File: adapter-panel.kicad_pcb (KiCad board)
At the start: 2 copper layers, 61 x 98.9 mm, 8 parts, among them J1 GPIB_Connector, U1 ArduioProMicro

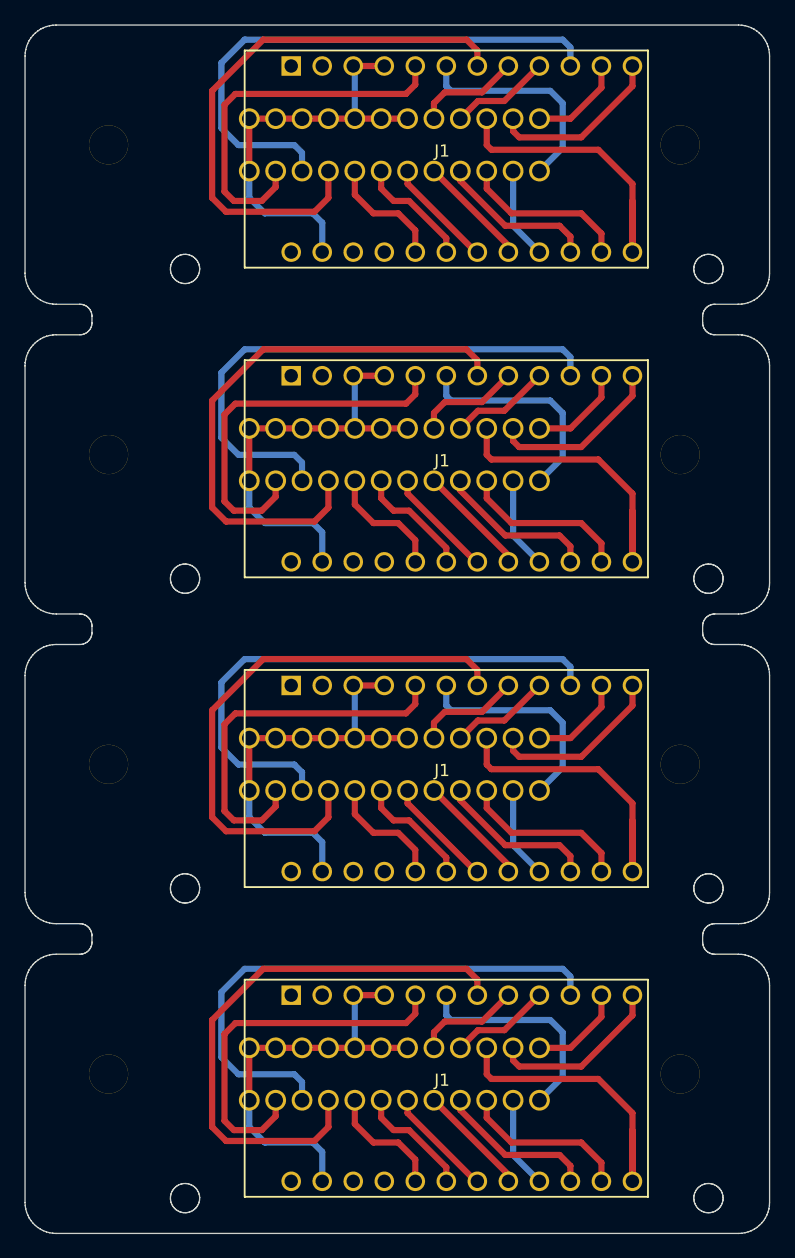
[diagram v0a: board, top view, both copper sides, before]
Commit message: switch from v-scores to mouse bites
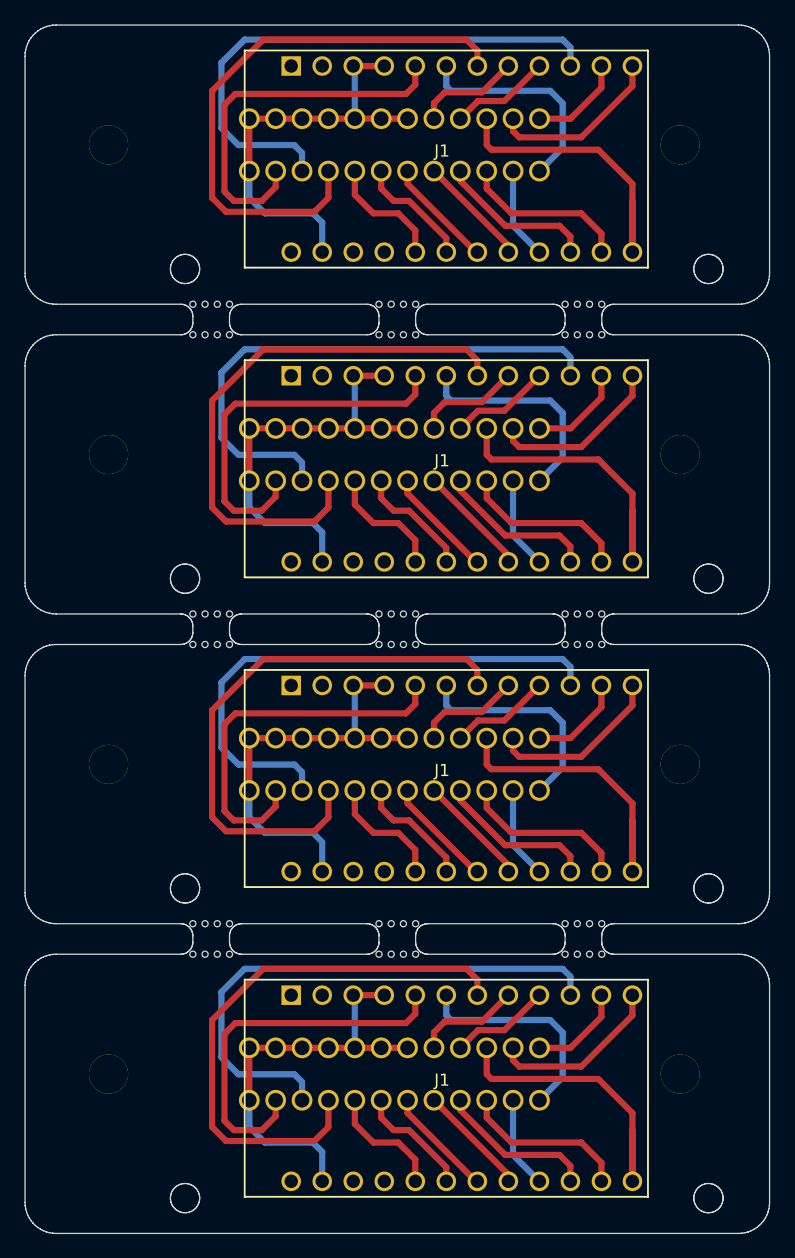
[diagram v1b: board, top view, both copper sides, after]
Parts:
- added REF**: NPTH, NPTH, F.Cu at (106.5, 138.8)
- added REF**: NPTH, NPTH, F.Cu at (75.0, 138.8)
- added REF**: NPTH, NPTH, F.Cu at (74.0, 138.8)
- added REF**: NPTH, NPTH, F.Cu at (73.0, 138.8)
- added REF**: NPTH, NPTH, F.Cu at (103.5, 136.3)
- added REF**: NPTH, NPTH, F.Cu at (104.5, 136.3)
- added REF**: NPTH, NPTH, F.Cu at (105.5, 136.3)
- added REF**: NPTH, NPTH, F.Cu at (106.5, 136.3)
- added REF**: NPTH, NPTH, F.Cu at (88.3, 136.3)
- added REF**: NPTH, NPTH, F.Cu at (89.3, 136.3)
- added REF**: NPTH, NPTH, F.Cu at (90.3, 136.3)
- added REF**: NPTH, NPTH, F.Cu at (105.5, 138.8)
- added REF**: NPTH, NPTH, F.Cu at (91.3, 136.3)
- added REF**: NPTH, NPTH, F.Cu at (73.0, 136.3)
- added REF**: NPTH, NPTH, F.Cu at (74.0, 136.3)
- added REF**: NPTH, NPTH, F.Cu at (75.0, 136.3)
- added REF**: NPTH, NPTH, F.Cu at (76.0, 136.3)
- added REF**: NPTH, NPTH, F.Cu at (106.5, 113.5)
- added REF**: NPTH, NPTH, F.Cu at (105.5, 113.5)
- added REF**: NPTH, NPTH, F.Cu at (104.5, 113.5)
- added REF**: NPTH, NPTH, F.Cu at (103.5, 113.5)
- added REF**: NPTH, NPTH, F.Cu at (91.3, 113.5)
- added REF**: NPTH, NPTH, F.Cu at (104.5, 138.8)
- added REF**: NPTH, NPTH, F.Cu at (90.3, 113.5)
- added REF**: NPTH, NPTH, F.Cu at (89.3, 113.5)
- added REF**: NPTH, NPTH, F.Cu at (88.3, 113.5)
- added REF**: NPTH, NPTH, F.Cu at (76.0, 113.5)
- added REF**: NPTH, NPTH, F.Cu at (75.0, 113.5)
- added REF**: NPTH, NPTH, F.Cu at (74.0, 113.5)
- added REF**: NPTH, NPTH, F.Cu at (73.0, 113.5)
- added REF**: NPTH, NPTH, F.Cu at (103.5, 111.0)
- added REF**: NPTH, NPTH, F.Cu at (104.5, 111.0)
- added REF**: NPTH, NPTH, F.Cu at (105.5, 111.0)
- added REF**: NPTH, NPTH, F.Cu at (103.5, 138.8)
- added REF**: NPTH, NPTH, F.Cu at (106.5, 111.0)
- added REF**: NPTH, NPTH, F.Cu at (88.3, 111.0)
- added REF**: NPTH, NPTH, F.Cu at (89.3, 111.0)
- added REF**: NPTH, NPTH, F.Cu at (90.3, 111.0)
- added REF**: NPTH, NPTH, F.Cu at (91.3, 111.0)
- added REF**: NPTH, NPTH, F.Cu at (73.0, 111.0)
- added REF**: NPTH, NPTH, F.Cu at (74.0, 111.0)
- added REF**: NPTH, NPTH, F.Cu at (75.0, 111.0)
- added REF**: NPTH, NPTH, F.Cu at (76.0, 111.0)
- added REF**: NPTH, NPTH, F.Cu at (106.5, 88.1)
- added REF**: NPTH, NPTH, F.Cu at (91.3, 138.8)
- added REF**: NPTH, NPTH, F.Cu at (105.5, 88.1)
- added REF**: NPTH, NPTH, F.Cu at (104.5, 88.1)
- added REF**: NPTH, NPTH, F.Cu at (103.5, 88.1)
- added REF**: NPTH, NPTH, F.Cu at (91.3, 88.1)
- added REF**: NPTH, NPTH, F.Cu at (90.3, 88.1)
- added REF**: NPTH, NPTH, F.Cu at (89.3, 88.1)
- added REF**: NPTH, NPTH, F.Cu at (88.3, 88.1)
- added REF**: NPTH, NPTH, F.Cu at (76.0, 88.1)
- added REF**: NPTH, NPTH, F.Cu at (75.0, 88.1)
- added REF**: NPTH, NPTH, F.Cu at (74.0, 88.1)
- added REF**: NPTH, NPTH, F.Cu at (90.3, 138.8)
- added REF**: NPTH, NPTH, F.Cu at (73.0, 88.1)
- added REF**: NPTH, NPTH, F.Cu at (103.5, 85.6)
- added REF**: NPTH, NPTH, F.Cu at (104.5, 85.6)
- added REF**: NPTH, NPTH, F.Cu at (105.5, 85.6)
- added REF**: NPTH, NPTH, F.Cu at (106.5, 85.6)
- added REF**: NPTH, NPTH, F.Cu at (88.3, 85.6)
- added REF**: NPTH, NPTH, F.Cu at (89.3, 85.6)
- added REF**: NPTH, NPTH, F.Cu at (90.3, 85.6)
- added REF**: NPTH, NPTH, F.Cu at (91.3, 85.6)
- added REF**: NPTH, NPTH, F.Cu at (73.0, 85.6)
- added REF**: NPTH, NPTH, F.Cu at (89.3, 138.8)
- added REF**: NPTH, NPTH, F.Cu at (74.0, 85.6)
- added REF**: NPTH, NPTH, F.Cu at (75.0, 85.6)
- added REF**: NPTH, NPTH, F.Cu at (76.0, 85.6)
- added REF**: NPTH, NPTH, F.Cu at (88.3, 138.8)
- added REF**: NPTH, NPTH, F.Cu at (76.0, 138.8)
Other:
- outline, holes or cut-outs redrawn
- board text removed: "V-CUT"
